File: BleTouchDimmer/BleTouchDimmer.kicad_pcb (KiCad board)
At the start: 2 copper layers, 65 parts, among them J1 Conn_01x03, J2 Conn_01x03, J3 JTAG, J4 Conn_01x06, J5 SLIDER1, J6 SLIDER2, P3 POWER, Q1 PDTC123J, Q2 PDTC123J, Q3 PDTC123J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

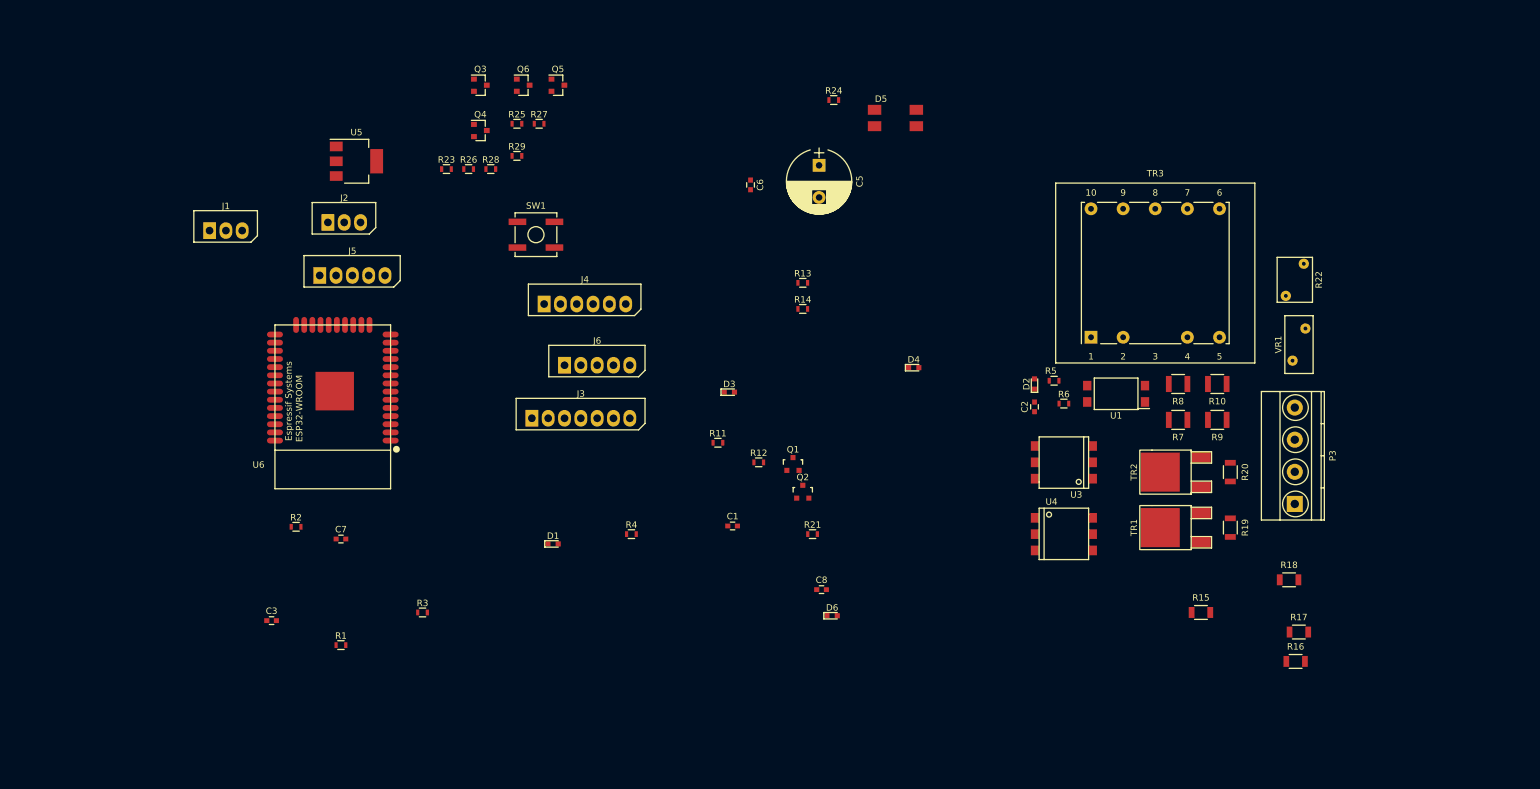
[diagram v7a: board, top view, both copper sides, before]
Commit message: Started larger pcb with 2 slider wheel PCBs.
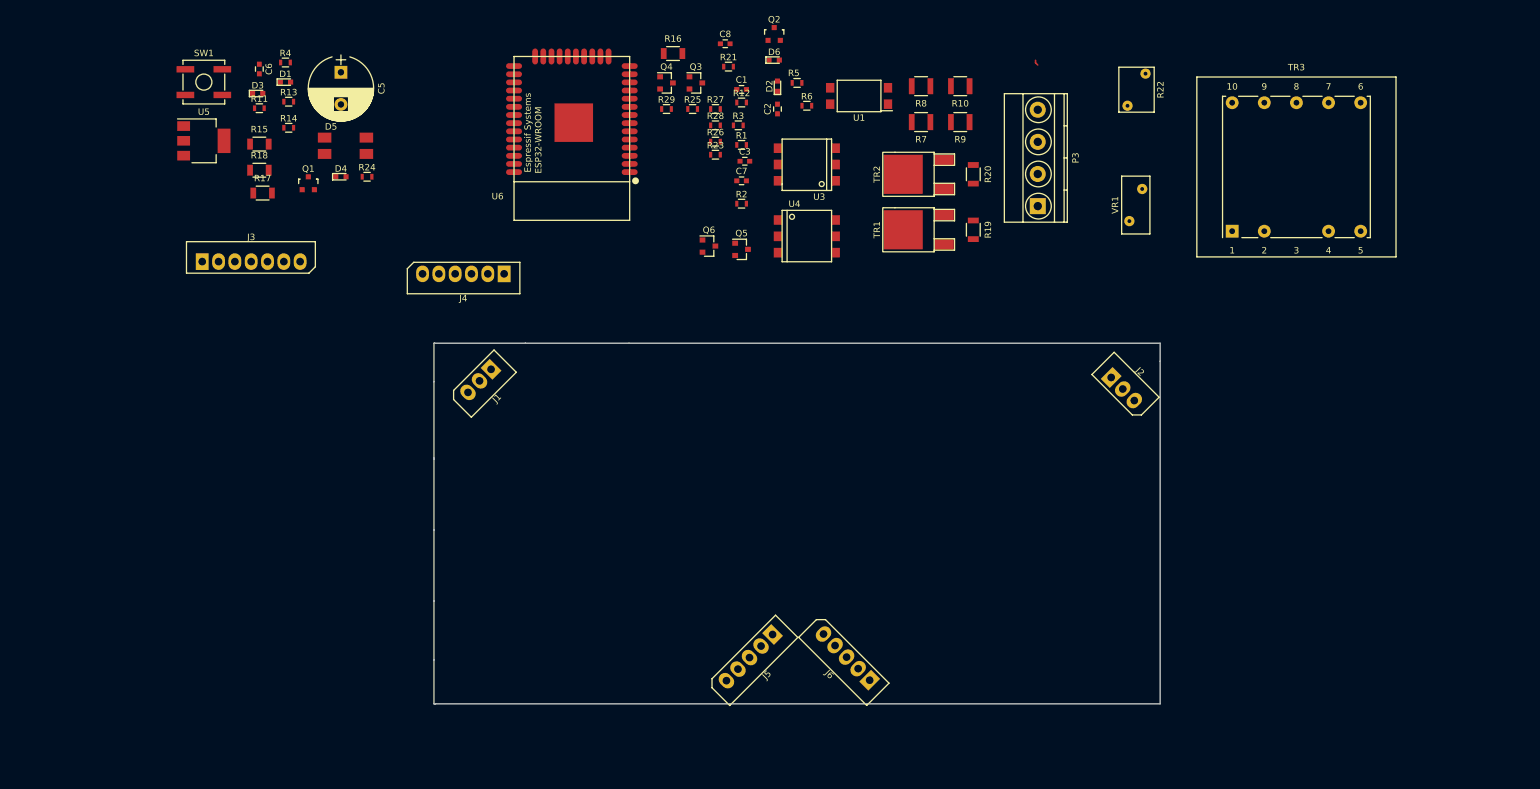
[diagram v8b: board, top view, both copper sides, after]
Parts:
- moved R17 175.2 mm to (77.5, 39.9)
- moved R18 172.5 mm to (77.0, 36.3)
- moved R15 163.7 mm to (77.0, 32.3)
- moved R16 135.4 mm to (141.4, 18.2)
- moved J2 124.3 mm to (209.6, 68.6), turned to 315 degrees
- moved C3 102.7 mm to (152.5, 34.9)
- moved R1 99.7 mm to (152.0, 32.4)
- moved D4 94.0 mm to (89.7, 37.3)
- moved R4 91.0 mm to (81.0, 19.6)
- moved R3 90.4 mm to (151.5, 29.3)
- moved J5 89.9 mm to (156.8, 108.6), turned to 225 degrees
- moved R11 88.3 mm to (77.0, 26.7)
- moved Q1 87.2 mm to (84.6, 38.4)
- moved D6 87.0 mm to (157.1, 19.2)
- moved D3 86.9 mm to (76.7, 24.4)
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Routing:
- net (no net): track 0.00 -> 0.89 mm
- net /N: track 0.89 -> 0.00 mm
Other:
- board outline added: 113 x 56.1 mm
